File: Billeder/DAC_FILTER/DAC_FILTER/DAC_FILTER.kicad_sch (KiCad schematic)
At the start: 66 parts, among them U1 LTC1668, U2 OPA4830, U3 OPA4830

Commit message: DC power amp calculations
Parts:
- removed C1, C3: 3n3, symbol Device:C
- removed C10, C20: 19p6, symbol Device:C
- removed C11, C14, C17, C19, C21, C5, C7, C9: 10p, symbol Device:C
- removed C12, C22: 20p5, symbol Device:C
- removed C13, C16: 1u, symbol Device:C
- removed C15, C6: 10p5, symbol Device:C
- removed C18, C8: 16p2, symbol Device:C
- removed C2, C4: 820p, symbol Device:C
- removed L1, L3: 8u2, symbol Device:L
- removed L2, L4: 5u6, symbol Device:L
- removed L5: Common Mode Choke, symbol Device:L_Ferrite_Coupled_1324
- removed R1, R2: 50, symbol Device:R_US
- removed R10, R14, R18, R21, R28, R32, R36, R5: 1k24, symbol Device:R_US
- removed R11, R29: 12k4, symbol Device:R_US
- removed R12, R30: 2k21, symbol Device:R_US
- removed R13, R17, R20, R27, R31, R35, R4, R9: 2k49, symbol Device:R_US
- removed R15, R33: 18k7, symbol Device:R_US
- removed R16, R34: 1k02, symbol Device:R_US
- removed R19, R24: 20k, symbol Device:R_US
- removed R22, R6: 15k, symbol Device:R_US
- removed R23, R3: 23k2, symbol Device:R_US
- removed R25, R7: 13k7, symbol Device:R_US
- removed R26, R8: 4k75, symbol Device:R_US
- removed U1: LTC1668, symbol JFT_DAC:LTC1668
- removed unit 4 of U2
- removed unit 1 of U2
- removed unit 2 of U2
- removed unit 3 of U2
- removed unit 2 of U3
- removed unit 1 of U3
- removed unit 3 of U3
- removed unit 4 of U3
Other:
- added sheet DAC_AMP_SCHEMATIC (DAC_AMP_SCHEMATIC.kicad_sch)
- added sheet DAC_FILTER_SECTION (DAC_FILTER_SECTION.kicad_sch)
- note removed: "Out+"
- note removed: "Out-"

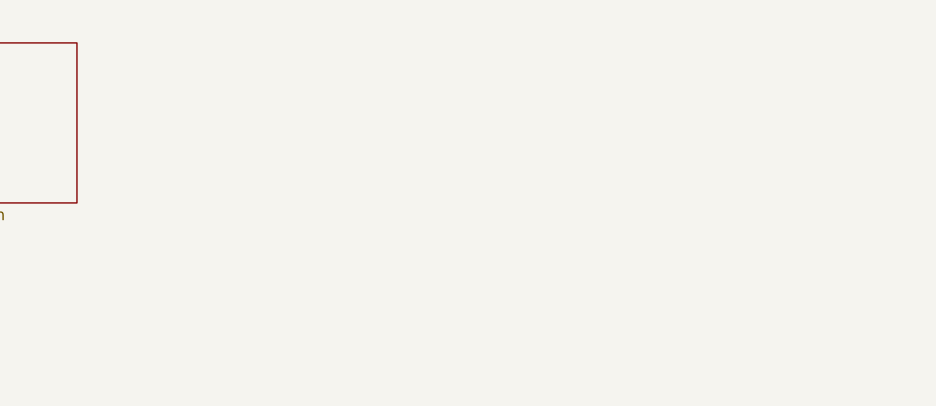
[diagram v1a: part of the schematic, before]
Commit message: DAC power amp stability
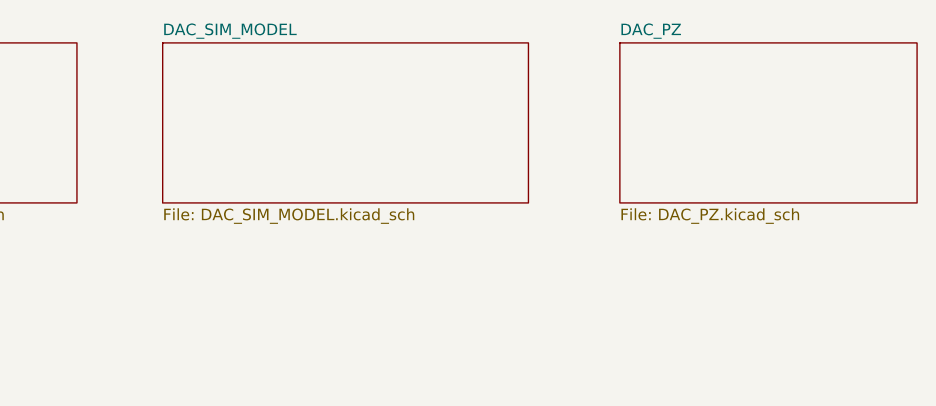
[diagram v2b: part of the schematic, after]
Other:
- added sheet DAC_PZ (DAC_PZ.kicad_sch)
- added sheet DAC_SIM_MODEL (DAC_SIM_MODEL.kicad_sch)
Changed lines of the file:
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@@
+	)
+	(sheet
+		(at 123.825 26.67)
+		(size 40.64 17.78)
+		(fields_autoplaced yes)
+		(stroke
+			(width 0.1524)
+			(type solid)
+		)
+		(fill
+			(color 0 0 0 0.0000)
+		)
+		(property "Sheetname" "DAC_SIM_MODEL"
+			(at 123.825 25.9584 0)
+			(effects
+				(font
+					(size 1.27 1.27)
+				)
+				(justify left bottom)
+			)
+		)
+		(property "Sheetfile" "DAC_SIM_MODEL.kicad_sch"
+			(at 123.825 45.0346 0)
+			(effects
+				(font
+					(size 1.27 1.27)
+				)
+				(justify left top)
+			)
+		)
+		(instances
+			(project "DAC_FILTER"
+				(path "/5ea4bdd8-845d-49bd-9427-a30bfd0e620f"
+					(page "4")
+				)
+			)
+		)
 	)
 	(sheet
@@
 				)
 			)
+		)
+	)
+	(sheet
+		(at 174.625 26.67)
+		(size 33.02 17.78)
+		(fields_autoplaced yes)
+		(stroke
+			(width 0.1524)
+			(type solid)
+		)
+		(fill
+			(color 0 0 0 0.0000)
+		)
+		(property "Sheetname" "DAC_PZ"
+			(at 174.625 25.9584 0)
+			(effects
+				(font
+					(size 1.27 1.27)
+				)
+				(justify left bottom)
+			)
+		)
+		(property "Sheetfile" "DAC_PZ.kicad_sch"
+			(at 174.625 45.0346 0)
+			(effects
+				(font
+					(size 1.27 1.27)
+				)
+				(justify left top)
+			)
+		)
+		(instances
+			(project "DAC_FILTER"
+				(path "/5ea4bdd8-845d-49bd-9427-a30bfd0e620f"
+					(page "5")
+				)
+			)
